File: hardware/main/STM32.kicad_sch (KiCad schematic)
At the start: 29 parts, among them U201 REF3430QDGKRQ1, U202 STM32L431RCTx

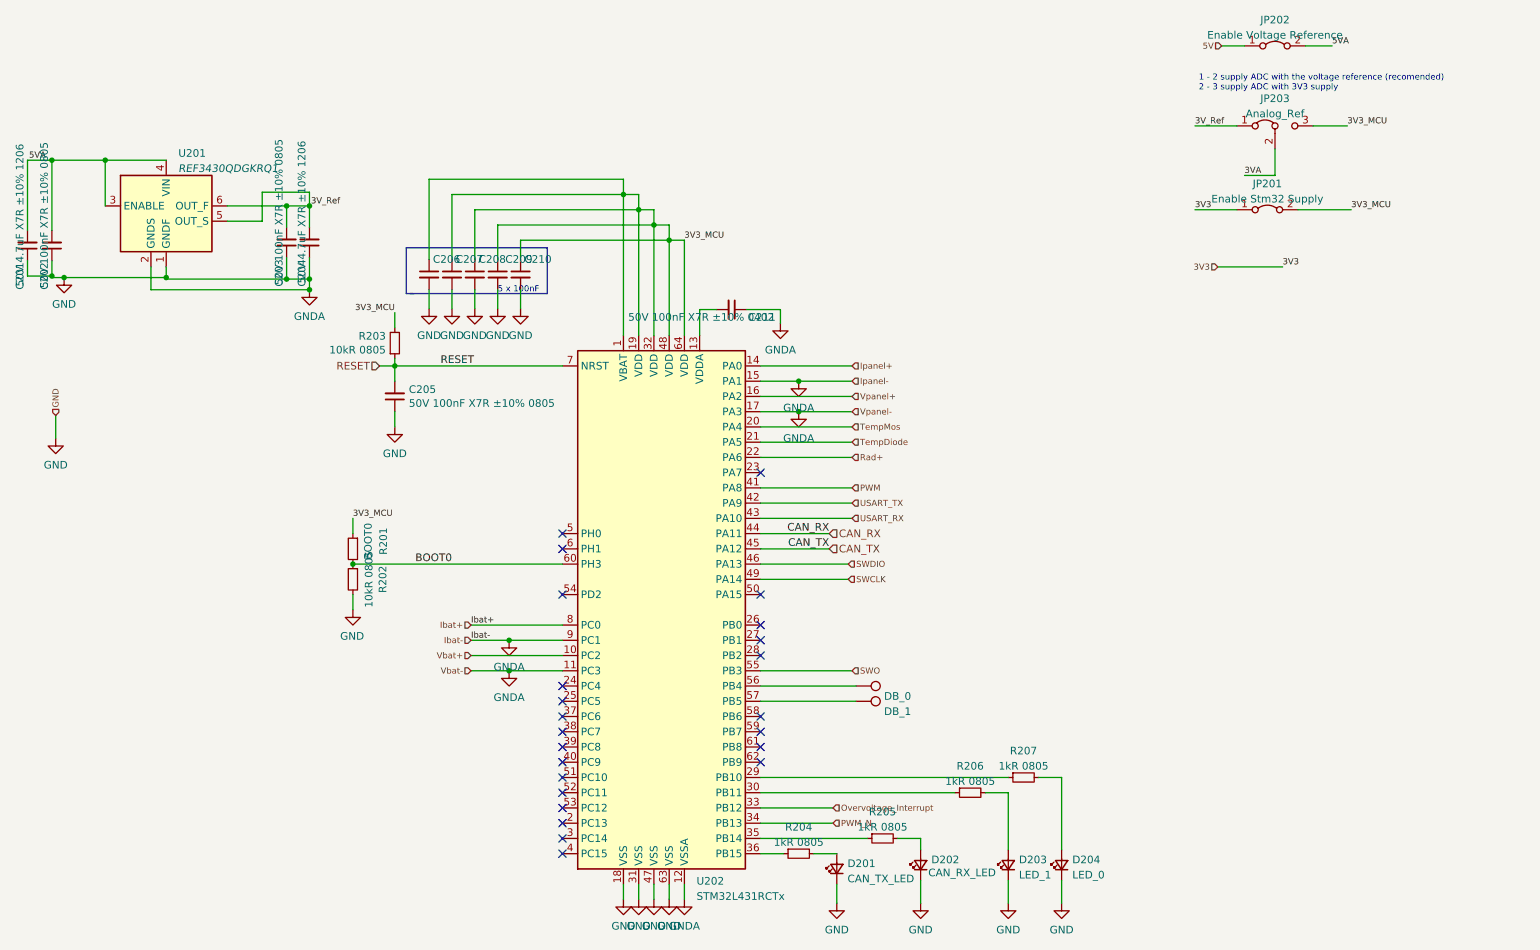
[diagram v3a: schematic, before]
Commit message: Schematics: Run DRC and fix errors and some warnings, also added Zenite kicad library repo as submodule
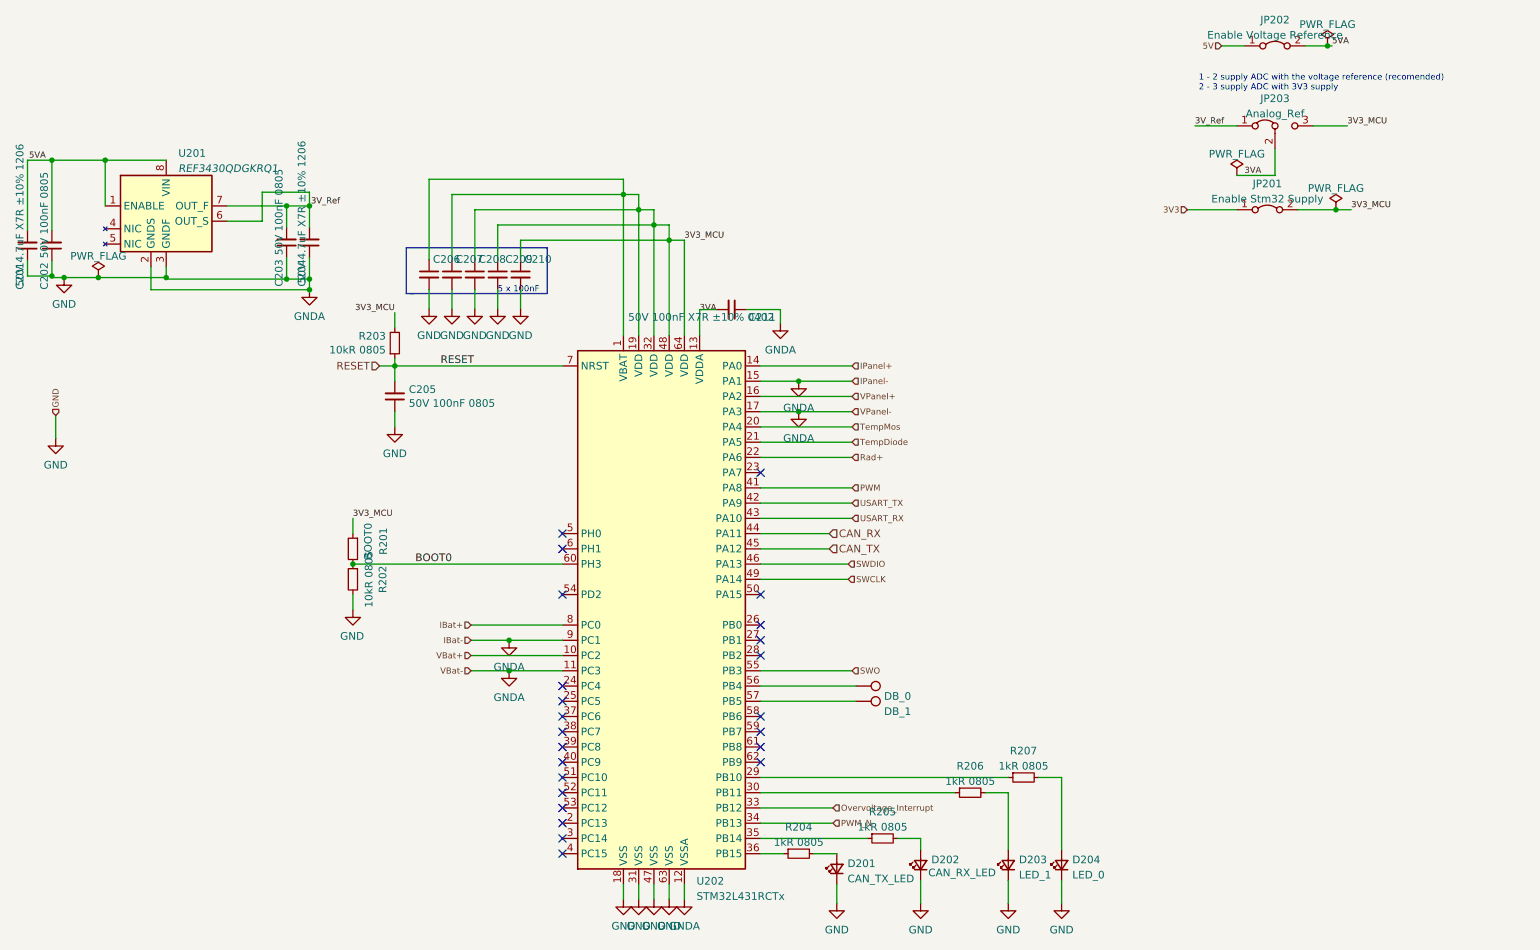
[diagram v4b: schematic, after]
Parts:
- removed U201: REF3430QDGKRQ1, Package_SO:VSSOP-8_3.0x3.0mm_P0.65mm, symbol Reference_Voltage:REF3220AMDBVREP
- added U201: REF3430QDGKRQ1, Package_SO:VSSOP-8_3.0x3.0mm_P0.65mm, symbol zenite:REF3430QDGKRQ1
- C201, C204: footprint (none) -> Capacitor_SMD:C_1206_3216Metric_Pad1.33x1.80mm_HandSolder
- C202, C203, C205: value 50V 100nF X7R ±10% 0805 -> 50V 100nF 0805; footprint (none) -> Capacitor_SMD:C_0805_2012Metric_Pad1.18x1.45mm_HandSolder
- C206, C207, C208, C209, C210, C211: footprint (none) -> Capacitor_SMD:C_0402_1005Metric_Pad0.74x0.62mm_HandSolder
- D201, D202, D203, D204: footprint (none) -> LED_SMD:LED_0805_2012Metric_Pad1.15x1.40mm_HandSolder
- JP201, JP202: footprint (none) -> Jumper:SolderJumper-2_P1.3mm_Open_TrianglePad1.0x1.5mm
- JP203: footprint (none) -> Jumper:SolderJumper-3_P1.3mm_Open_Pad1.0x1.5mm
- R203, R204, R205, R206, R207: footprint (none) -> Resistor_SMD:R_0805_2012Metric_Pad1.20x1.40mm_HandSolder
- TP201, TP202: footprint (none) -> TestPoint:TestPoint_Pad_2.0x2.0mm
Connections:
- net 3VA: now also C211.2, U202.13 (VDDA)
- net 3V_Ref: now also U201.6 (OUT_S), U201.7 (OUT_F)
- net 5VA: now also U201.1 (ENABLE), U201.8 (VIN)
- net GND: now also U201.2 (GNDS), U201.3 (GNDF)
- net Ibat+ renamed IBat+
- net Ipanel+ renamed IPanel+
- net Vbat+ renamed VBat+
- net Vpanel+ renamed VPanel+

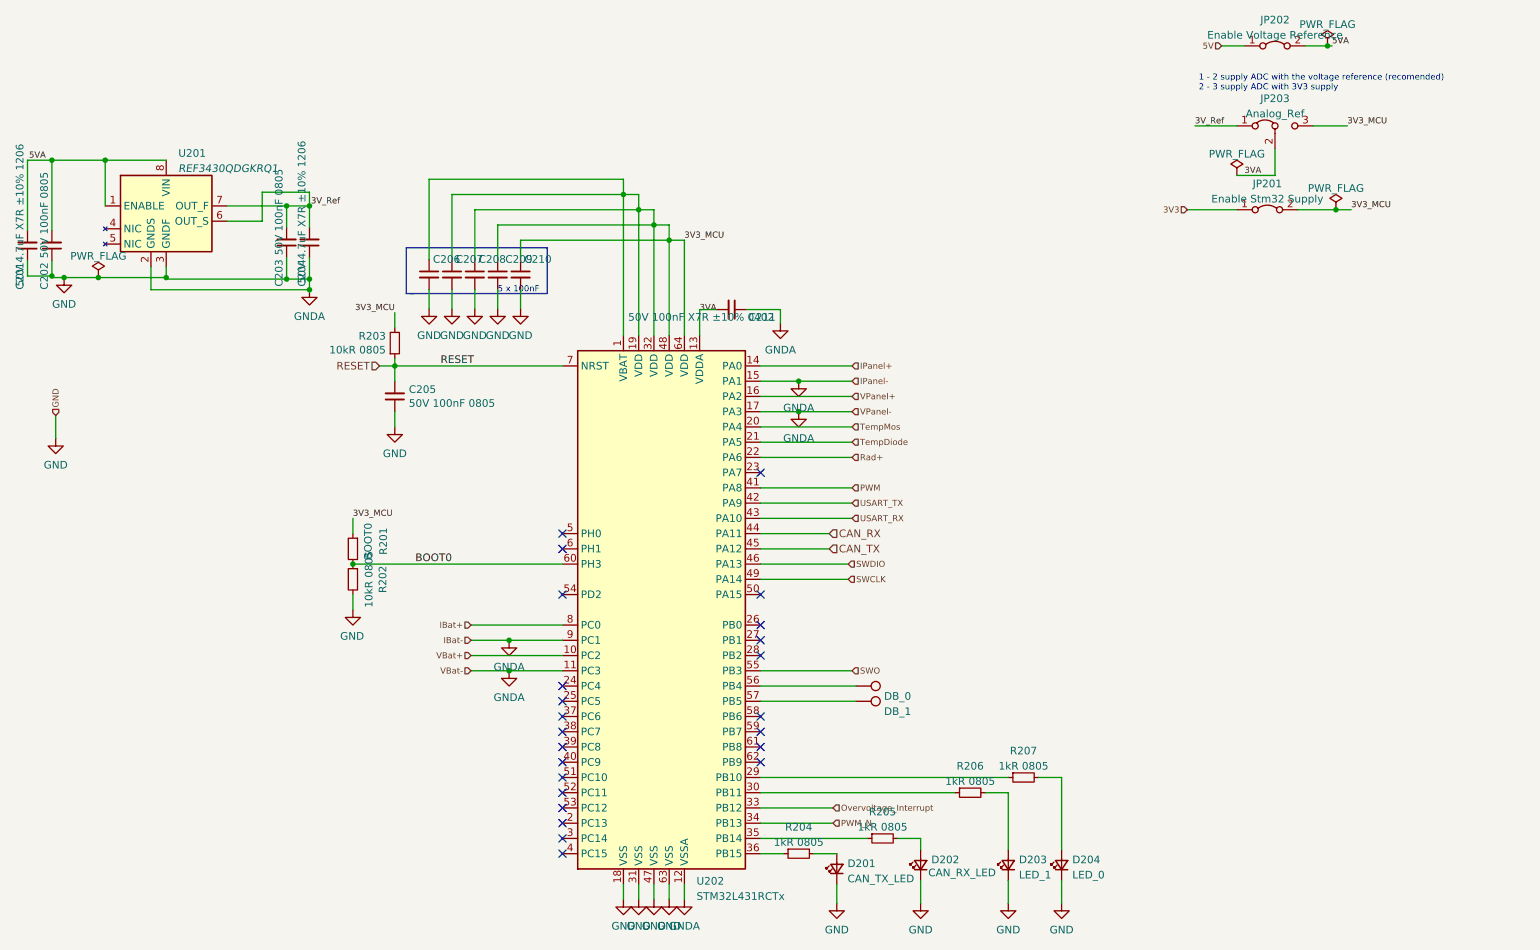
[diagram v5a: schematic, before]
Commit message: Schematics: Add STM32 comparator for Battery OverVoltage
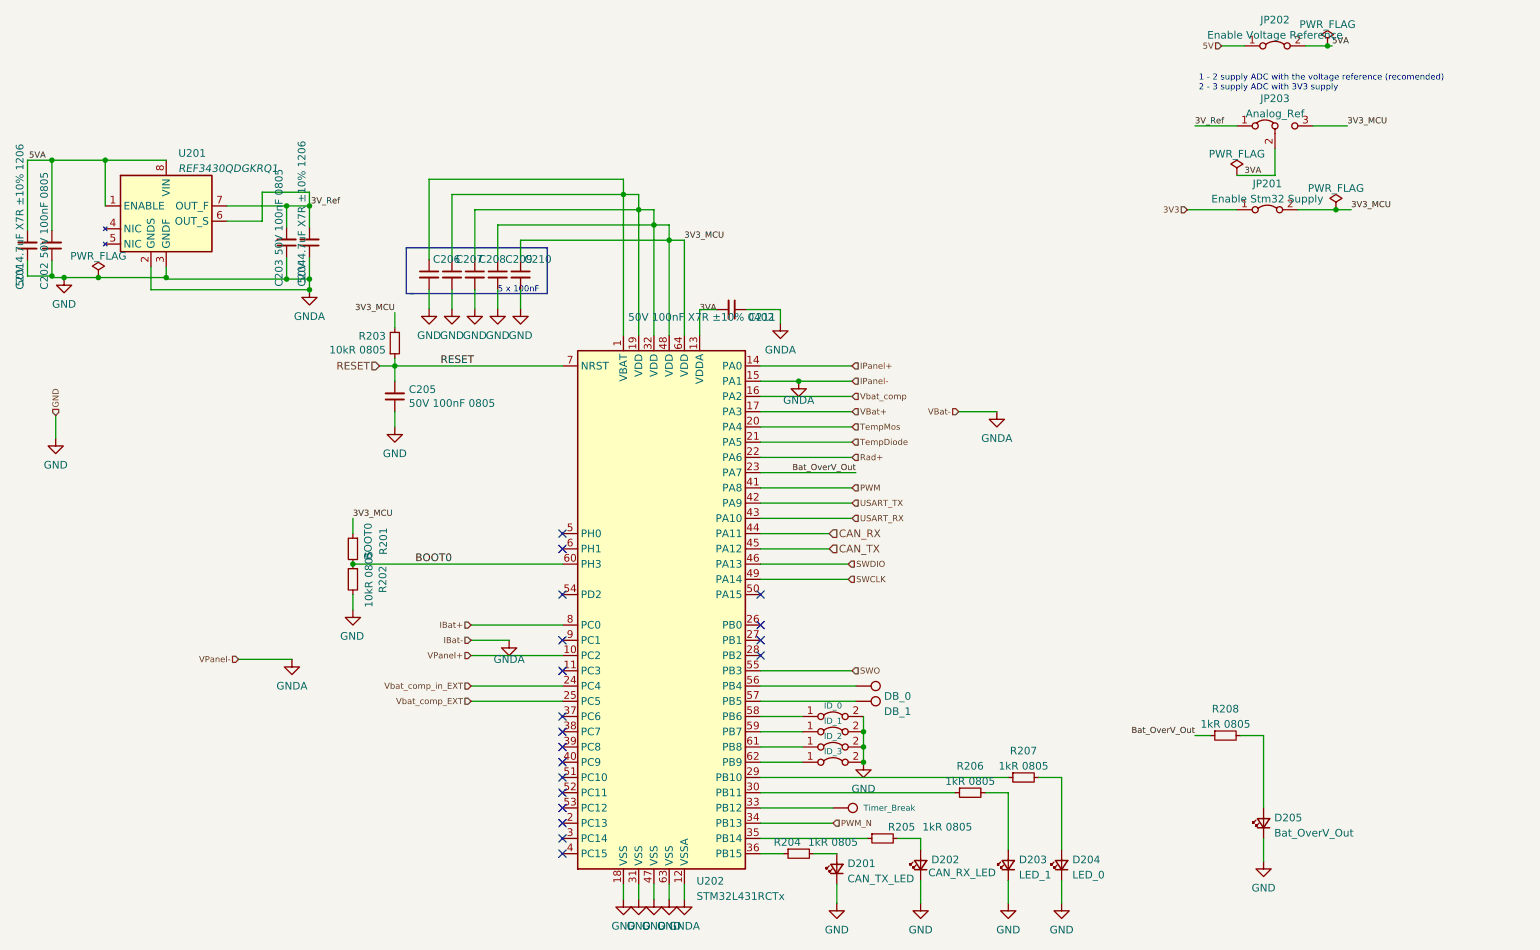
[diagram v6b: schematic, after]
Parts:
- added D205: Bat_OverV_Out, LED_SMD:LED_0805_2012Metric_Pad1.15x1.40mm_HandSolder, symbol Device:LED_Small
- added JP204: ID_0, Jumper:SolderJumper-2_P1.3mm_Open_TrianglePad1.0x1.5mm, symbol Jumper:Jumper_2_Bridged
- added JP205: ID_1, Jumper:SolderJumper-2_P1.3mm_Open_TrianglePad1.0x1.5mm, symbol Jumper:Jumper_2_Bridged
- added JP206: ID_2, Jumper:SolderJumper-2_P1.3mm_Open_TrianglePad1.0x1.5mm, symbol Jumper:Jumper_2_Bridged
- added JP207: ID_3, Jumper:SolderJumper-2_P1.3mm_Open_TrianglePad1.0x1.5mm, symbol Jumper:Jumper_2_Bridged
- added R208: 1kR 0805, Resistor_SMD:R_0805_2012Metric_Pad1.20x1.40mm_HandSolder, symbol Device:R_Small
- added TP203: Timer_Break, TestPoint:TestPoint_Pad_2.0x2.0mm, symbol Connector:TestPoint
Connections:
- net GND: now also D205.1 (K), JP204.2 (B), JP205.2 (B), JP206.2 (B), JP207.2 (B); no longer U202.11 (PC3), U202.17 (PA3), U202.9 (PC1)
- net VBat+: now also U202.17 (PA3); no longer U202.10 (PC2)
- net VPanel+: now also U202.10 (PC2); no longer U202.16 (PA2)
- net Bat_OverV_Out: now reaches U202.23 (PA7)
- net Bat_OverV_Out: now also R208.1
- net Vbat_comp_in_EXT: now reaches U202.24 (PC4)
- net Vbat_comp_EXT: now reaches U202.25 (PC5)
- net at U202.58 (PB6): now also JP204.1 (A)
- net at U202.59 (PB7): now also JP205.1 (A)
- net at U202.61 (PB8): now also JP206.1 (A)
- net at U202.62 (PB9): now also JP207.1 (A)
- net Overvoltage_Interrupt: no longer names the net of U202.33 (PB12)
- net Overvoltage_Interrupt: now also TP203.1
- new net: D205.2 (A), R208.2
- new net Vbat_comp: U202.16 (PA2)
- no-connect marks 24 -> 19
